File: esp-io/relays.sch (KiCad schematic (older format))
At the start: 35 parts, among them Q1 NPN, Q2 NPN, Q3 NPN, Q4 NPN, Q5 NPN, U3 SONGLE_RELAY_10A, U4 SONGLE_RELAY_10A, U5 SONGLE_RELAY_10A, U6 SONGLE_RELAY_10A, U7 SONGLE_RELAY_10A

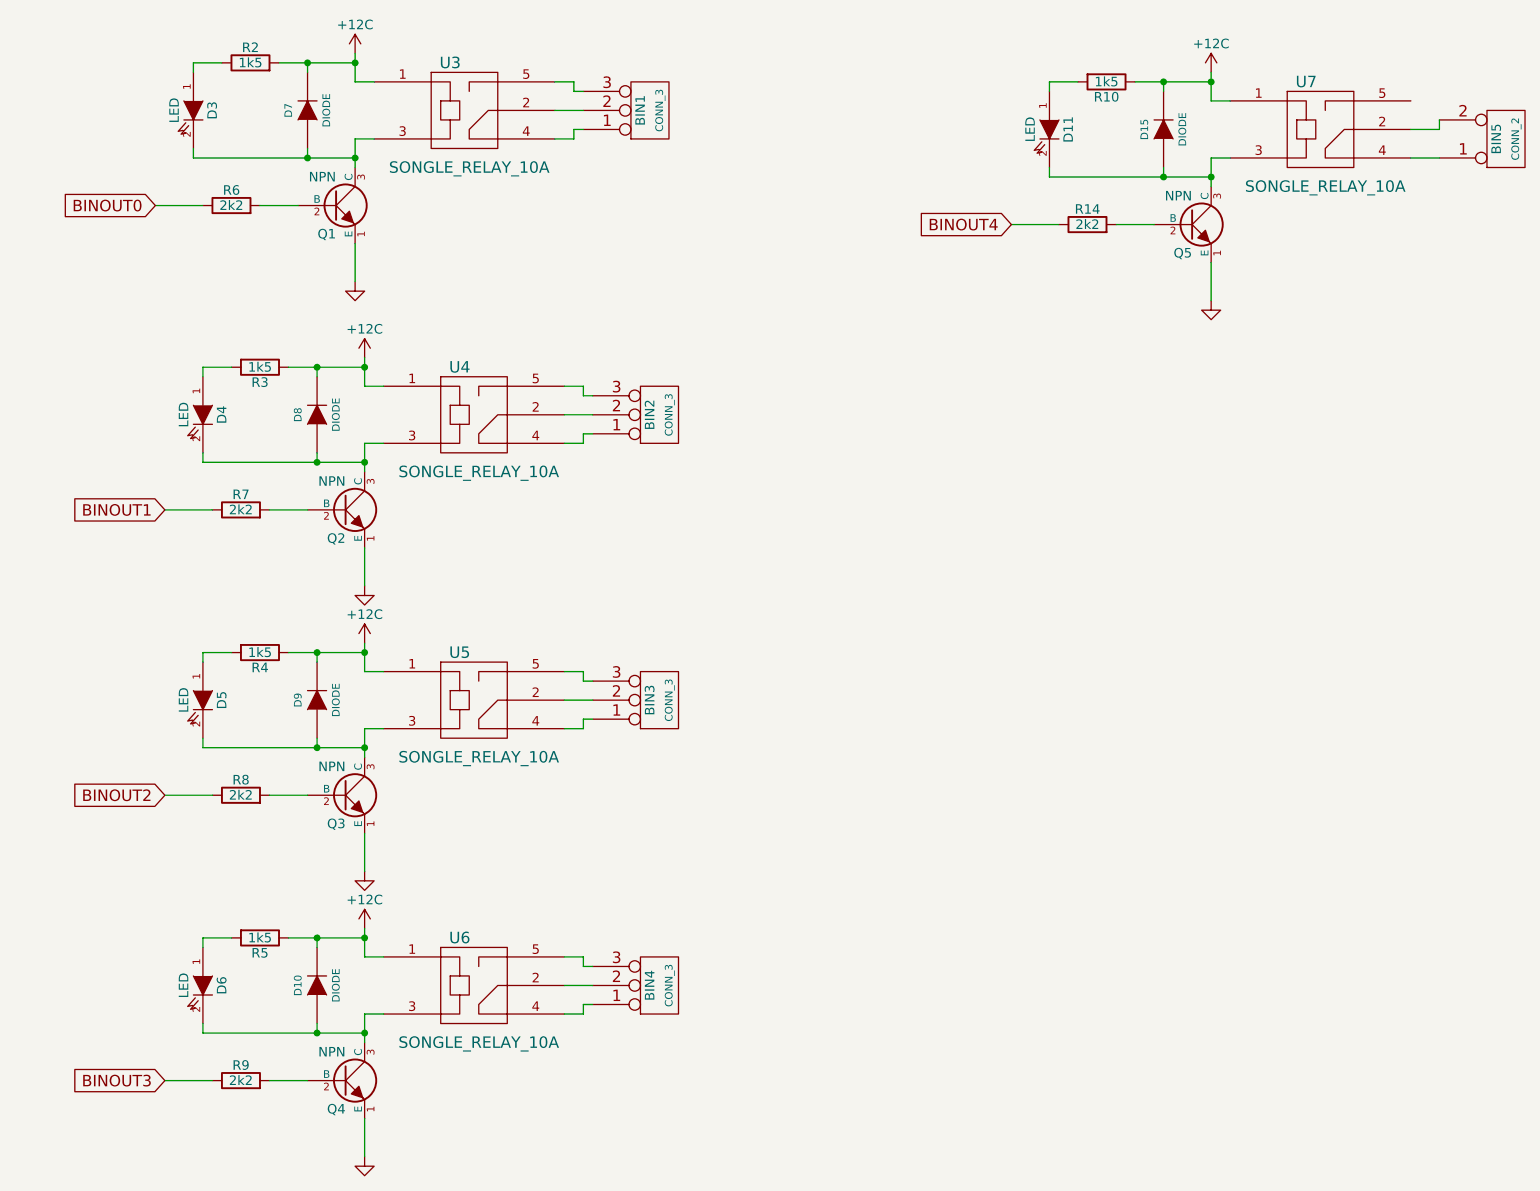
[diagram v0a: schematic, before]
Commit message: fifth relay removed
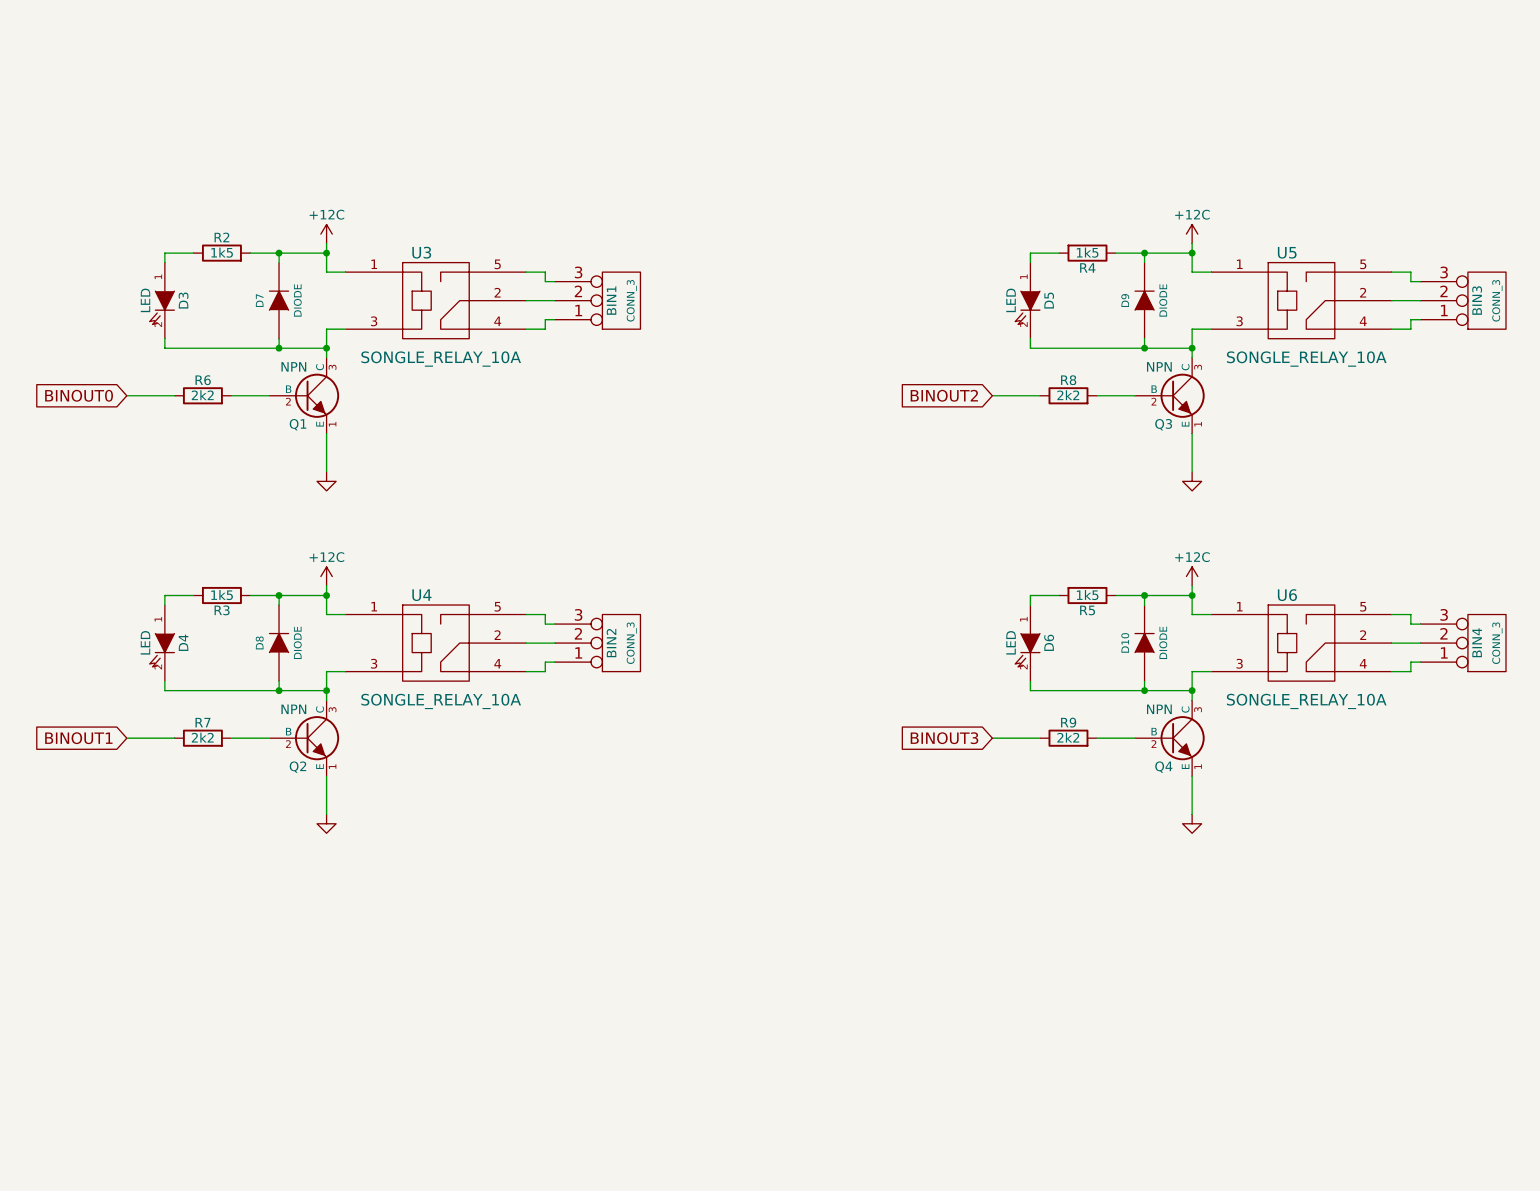
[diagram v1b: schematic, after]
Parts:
- removed BIN5: CONN_2, myconnectors:terminal_block_5mm_2P, symbol CONN_2
- removed D11: LED, mysmd:SM0603S_POL, symbol LED-RESCUE-rcu-board
- removed D15: DIODE, mysmd:SOD323, symbol DIODE
- removed Q5: NPN, libcms:SOT23EBC, symbol NPN
- removed R10: 1k5, mysmd:SM0603S, symbol R
- removed R14: 2k2, mysmd:SM0603S, symbol R
- removed U7: SONGLE_RELAY_10A, mymods:SONGLE_RELAY_10A, symbol SONGLE_RELAY_10A
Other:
- moved on the sheet: BIN1, BIN2, BIN3, BIN4, D10, D3, D4, D5, D6, D7, D8, D9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
